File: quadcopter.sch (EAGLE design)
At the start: 69 parts, among them J4 AVR_SPI_PRG_6NS, M1 MOTOR_PADS, M2 MOTOR_PADS, M3 MOTOR_PADS, M4 MOTOR_PADS, U1 ATMEGA128RFA1

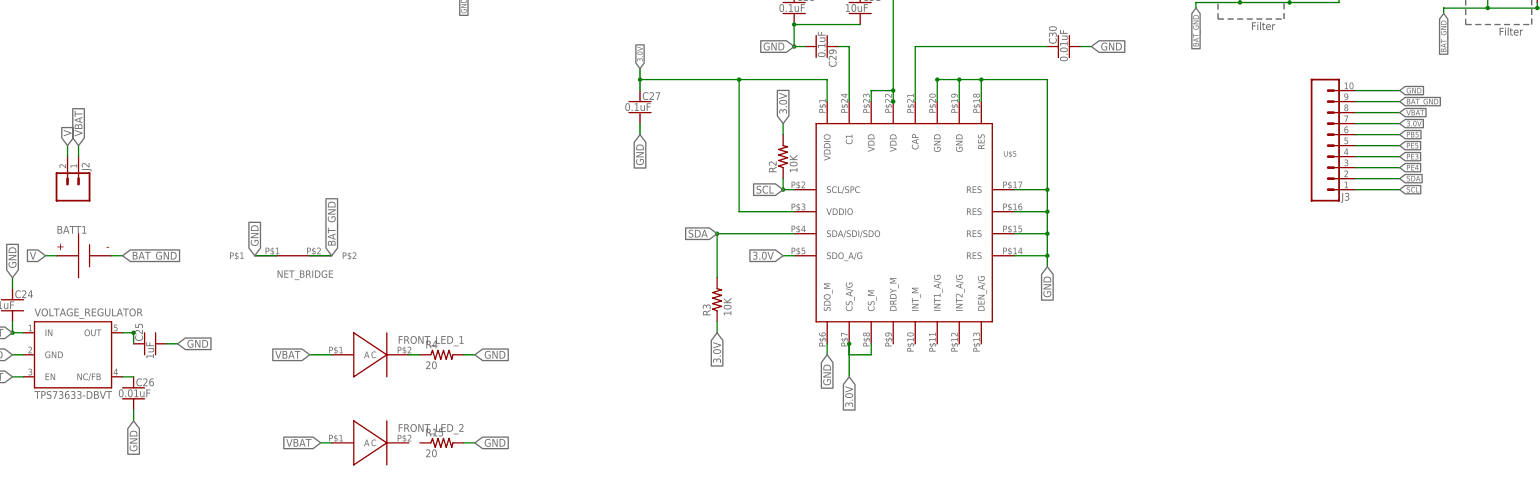
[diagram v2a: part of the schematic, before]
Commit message: Added all parts to board but have yet to run autorouter/set up the traces
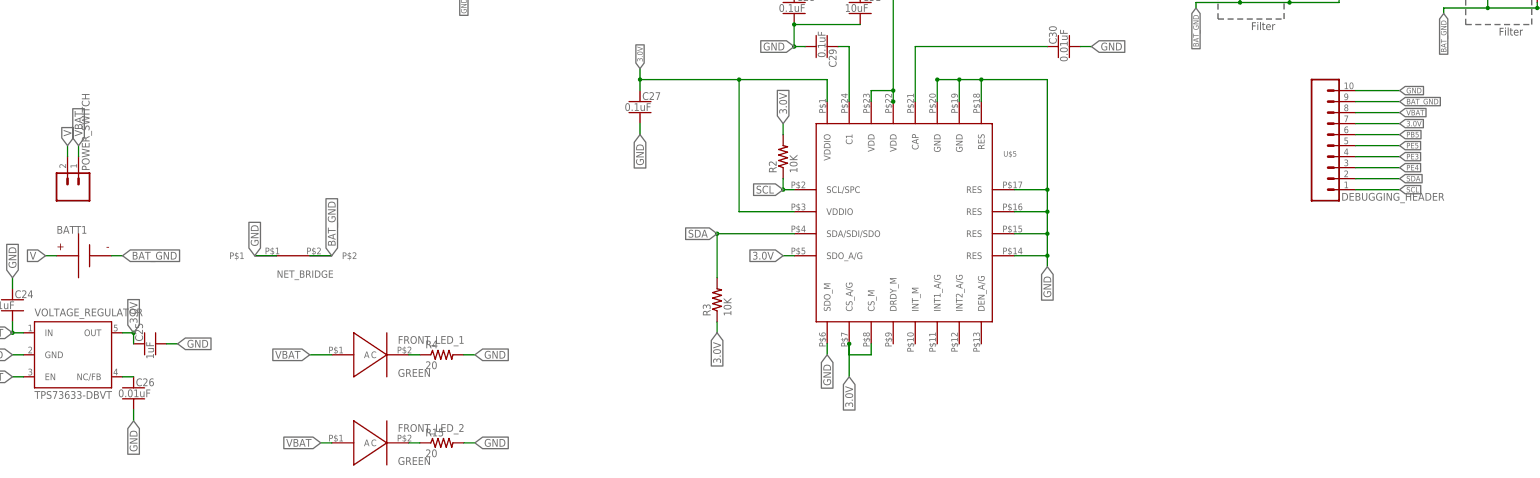
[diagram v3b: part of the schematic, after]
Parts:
- FRONT_LED_1, FRONT_LED_2: value (none) -> GREEN
- renumbered J2 to POWER_SWITCH, J3 to DEBUGGING_HEADER
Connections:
- new net N$5: FRONT_LED_2.C, R15.1
- net DTR: now also JP2.1
- net GND: now also JP2.6, JP3.6
- net RX0: now also JP2.3
- net RX1: now also JP3.2
- net TX0: now also JP2.2
- net TX1: now also JP3.3
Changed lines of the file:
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@@
 <setting verticaltext="up"/>
 </settings>
-<grid distance="0.05" unitdist="inch" unit="inch" style="lines" multiple="1" display="no" altdistance="0.01" altunitdist="inch" altunit="inch"/>
+<grid distance="0.1" unitdist="inch" unit="inch" style="lines" multiple="1" display="no" altdistance="0.01" altunitdist="inch" altunit="inch"/>
 <layers>
 <layer number="1" name="Top" color="4" fill="1" visible="no" active="no"/>
@@
 <part name="U$5" library="quadparts_jay" deviceset="IMU_497-14946-1-ND" device=""/>
 <part name="BATT1" library="quadparts_prebuilt" deviceset="BATTERY" device="-HUBSAN-W/HOLDER"/>
-<part name="J2" library="quadparts_jay" deviceset="MALE_HEADER_2POS" device="-2X1-0.1IN"/>
+<part name="POWER_SWITCH" library="quadparts_jay" deviceset="MALE_HEADER_2POS" device="-2X1-0.1IN"/>
 <part name="VOLTAGE_REGULATOR" library="quadparts_prebuilt" deviceset="TPS73633-DBVT" device=""/>
 <part name="NET_BRIDGE" library="quadparts_jay" deviceset="NET_BRIDGE" device=""/>
@@
 <part name="C6" library="quadparts_prebuilt" deviceset="CAPACITOR-NP_" device="SMD-2012-0805_CERAMIC-22PF" value="22pF"/>
 <part name="B2" library="quadparts_prebuilt" deviceset="BALUN" device="0805"/>
-<part name="J3" library="quadparts_prebuilt" deviceset="SIP-10_" device="TH-254X10-1"/>
-<part name="FRONT_LED_1" library="LEDs" deviceset="LED" device="-0805-GREEN"/>
-<part name="FRONT_LED_2" library="LEDs" deviceset="LED" device="-0805-GREEN"/>
+<part name="DEBUGGING_HEADER" library="quadparts_prebuilt" deviceset="SIP-10_" device="TH-254X10-1"/>
+<part name="FRONT_LED_1" library="LEDs" deviceset="LED" device="-0805-GREEN" value="GREEN"/>
+<part name="FRONT_LED_2" library="LEDs" deviceset="LED" device="-0805-GREEN" value="GREEN"/>
 <part name="R2" library="quadparts_prebuilt" deviceset="RESISTOR_" device="SMD-2012-0805-10K" value="10K"/>
 <part name="R3" library="quadparts_prebuilt" deviceset="RESISTOR_" device="SMD-2012-0805-10K" value="10K"/>
@@
 <instance part="U$5" gate="G$1" x="193.04" y="-45.72"/>
 <instance part="BATT1" gate="G$1" x="5.08" y="-53.34"/>
-<instance part="J2" gate="G$1" x="5.08" y="-40.64" rot="R90"/>
+<instance part="POWER_SWITCH" gate="G$1" x="5.08" y="-40.64" rot="R90"/>
 <instance part="VOLTAGE_REGULATOR" gate="G$1" x="-7.62" y="-83.82"/>
 <instance part="NET_BRIDGE" gate="G$1" x="53.34" y="-53.34"/>
@@
 <instance part="C6" gate="G$1" x="129.54" y="83.82" rot="R90"/>
 <instance part="B2" gate="G$1" x="142.24" y="81.28" rot="R180"/>
-<instance part="J3" gate="G$1" x="287.02" y="-40.64"/>
+<instance part="DEBUGGING_HEADER" gate="G$1" x="287.02" y="-40.64"/>
 <instance part="FRONT_LED_1" gate="G$1" x="71.12" y="-76.2"/>
 <instance part="FRONT_LED_2" gate="G$1" x="71.12" y="-96.52"/>
@@
 <wire x1="185.42" y1="158.75" x2="187.96" y2="158.75" width="0.1524" layer="91"/>
 <label x="187.96" y="158.75" size="1.27" layer="95" xref="yes"/>
+<pinref part="JP3" gate="G$1" pin="6"/>
 </segment>
 <segment>
@@
 </segment>
 <segment>
-<pinref part="J3" gate="G$1" pin="10"/>
+<pinref part="DEBUGGING_HEADER" gate="G$1" pin="10"/>
 <wire x1="297.18" y1="-15.24" x2="307.34" y2="-15.24" width="0.1524" layer="91"/>
 <label x="307.34" y="-15.24" size="1.27" layer="95" xref="yes"/>
@@
 <wire x1="123.19" y1="152.4" x2="125.73" y2="152.4" width="0.1524" layer="91"/>
 <label x="125.73" y="152.4" size="1.27" layer="95" xref="yes"/>
+<pinref part="JP2" gate="G$1" pin="6"/>
 </segment>
 <segment>
@@
 </segment>
 <segment>
-<pinref part="J3" gate="G$1" pin="5"/>
+<pinref part="DEBUGGING_HEADER" gate="G$1" pin="5"/>
 <wire x1="297.18" y1="-27.94" x2="307.34" y2="-27.94" width="0.1524" layer="91"/>
 <label x="307.34" y="-27.94" size="1.27" layer="95" xref="yes"/>
@@
 </segment>
 <segment>
-<pinref part="J3" gate="G$1" pin="3"/>
+<pinref part="DEBUGGING_HEADER" gate="G$1" pin="3"/>
 <wire x1="297.18" y1="-33.02" x2="307.34" y2="-33.02" width="0.1524" layer="91"/>
 <label x="307.34" y="-33.02" size="1.27" layer="95" xref="yes"/>
@@
 </segment>
 <segment>
-<pinref part="J3" gate="G$1" pin="4"/>
+<pinref part="DEBUGGING_HEADER" gate="G$1" pin="4"/>
 <wire x1="297.18" y1="-30.48" x2="307.34" y2="-30.48" width="0.1524" layer="91"/>
 <label x="307.34" y="-30.48" size="1.27" layer="95" xref="yes"/>
@@
 <wire x1="123.19" y1="142.24" x2="142.24" y2="142.24" width="0.1524" layer="91"/>
 <label x="142.24" y="142.24" size="1.27" layer="95" xref="yes"/>
+<pinref part="JP2" gate="G$1" pin="2"/>
 </segment>
 </net>
@@
 <wire x1="123.19" y1="144.78" x2="142.24" y2="144.78" width="0.1524" layer="91"/>
 <label x="142.24" y="144.78" size="1.27" layer="95" xref="yes"/>
+<pinref part="JP2" gate="G$1" pin="3"/>
 </segment>
 </net>
@@
 <wire x1="185.42" y1="151.13" x2="187.96" y2="151.13" width="0.1524" layer="91"/>
 <label x="187.96" y="151.13" size="1.27" layer="95" xref="yes"/>
+<pinref part="JP3" gate="G$1" pin="3"/>
 </segment>
 </net>
@@
 <wire x1="185.42" y1="148.59" x2="187.96" y2="148.59" width="0.1524" layer="91"/>
 <label x="187.96" y="148.59" size="1.27" layer="95" xref="yes"/>
+<pinref part="JP3" gate="G$1" pin="2"/>
 </segment>
 </net>
@@
 </segment>
 <segment>
-<pinref part="J3" gate="G$1" pin="2"/>
+<pinref part="DEBUGGING_HEADER" gate="G$1" pin="2"/>
 <wire x1="297.18" y1="-35.56" x2="307.34" y2="-35.56" width="0.1524" layer="91"/>
 <label x="307.34" y="-35.56" size="1.27" layer="95" xref="yes"/>
@@
 </segment>
 <segment>
-<pinref part="J3" gate="G$1" pin="1"/>
+<pinref part="DEBUGGING_HEADER" gate="G$1" pin="1"/>
 <wire x1="297.18" y1="-38.1" x2="307.34" y2="-38.1" width="0.1524" layer="91"/>
 <label x="307.34" y="-38.1" size="1.27" layer="95" xref="yes"/>
@@
 </segment>
 <segment>
-<pinref part="J3" gate="G$1" pin="6"/>
+<pinref part="DEBUGGING_HEADER" gate="G$1" pin="6"/>
 <wire x1="297.18" y1="-25.4" x2="307.34" y2="-25.4" width="0.1524" layer="91"/>
 <label x="307.34" y="-25.4" size="1.27" layer="95" xref="yes"/>
@@
 <pinref part="C15" gate="G$1" pin="1"/>
 <wire x1="130.81" y1="139.7" x2="123.19" y2="139.7" width="0.1524" layer="91"/>
+<pinref part="JP2" gate="G$1" pin="1"/>
 </segment>
 </net>
@@
 </segment>
 <segment>
-<pinref part="J2" gate="G$1" pin="1"/>
+<pinref part="POWER_SWITCH" gate="G$1" pin="1"/>
 <wire x1="2.54" y1="-30.48" x2="2.54" y2="-27.94" width="0.1524" layer="91"/>
 <label x="2.54" y="-27.94" size="1.778" layer="95" rot="R90" xref="yes"/>
 </segment>
 <segment>
-<pinref part="J3" gate="G$1" pin="8"/>
+<pinref part="DEBUGGING_HEADER" gate="G$1" pin="8"/>
 <wire x1="297.18" y1="-20.32" x2="307.34" y2="-20.32" width="0.1524" layer="91"/>
 <label x="307.34" y="-20.32" size="1.27" layer="95" xref="yes"/>
@@
 <wire x1="15.24" y1="-71.12" x2="15.24" y2="-73.66" width="0.1524" layer="91"/>
 <pinref part="C25" gate="G$1" pin="1"/>
+<label x="15.24" y="-71.12" size="1.778" layer="95" rot="R90" xref="yes"/>
 </segment>
 <segment>
@@
 </segment>
 <segment>
-<pinref part="J3" gate="G$1" pin="7"/>
+<pinref part="DEBUGGING_HEADER" gate="G$1" pin="7"/>
 <wire x1="297.18" y1="-22.86" x2="307.34" y2="-22.86" width="0.1524" layer="91"/>
 <label x="307.34" y="-22.86" size="1.27" layer="95" xref="yes"/>
@@
 </segment>
 <segment>
-<pinref part="J3" gate="G$1" pin="9"/>
+<pinref part="DEBUGGING_HEADER" gate="G$1" pin="9"/>
 <wire x1="297.18" y1="-17.78" x2="307.34" y2="-17.78" width="0.1524" layer="91"/>
 <label x="307.34" y="-17.78" size="1.27" layer="95" xref="yes"/>
@@
 </segment>
 <segment>
-<pinref part="J2" gate="G$1" pin="2"/>
+<pinref part="POWER_SWITCH" gate="G$1" pin="2"/>
 <wire x1="0" y1="-30.48" x2="0" y2="-27.94" width="0.1524" layer="91"/>
 <label x="0" y="-27.94" size="1.778" layer="95" rot="R90" xref="yes"/>
@@
 </segment>
 </net>
+<net name="N$5" class="0">
+<segment>
+<pinref part="FRONT_LED_2" gate="G$1" pin="C"/>
+<pinref part="R15" gate="G$1" pin="1"/>
+<wire x1="78.74" y1="-96.52" x2="81.28" y2="-96.52" width="0.1524" layer="91"/>
+</segment>
+</net>
 </nets>
 </sheet>
 </sheets>
+<errors>
+</errors>
 </schematic>
 </drawing>

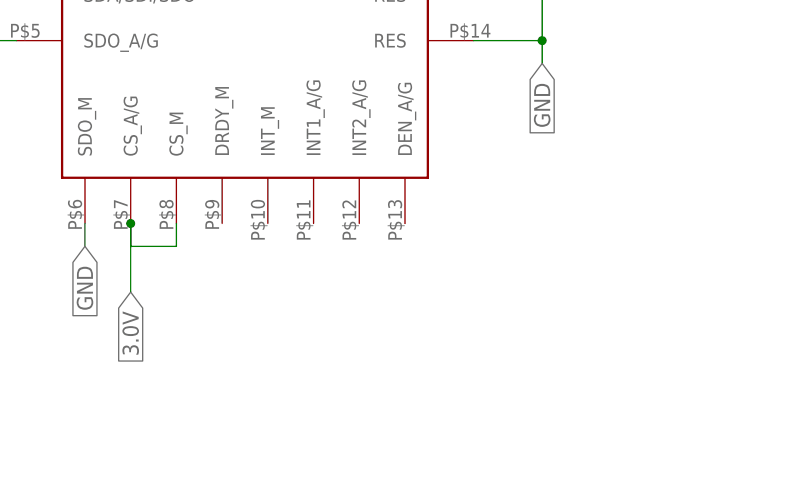
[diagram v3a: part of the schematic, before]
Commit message: Fixed some schematic things, still need to fix swanson notes and the motor drivers
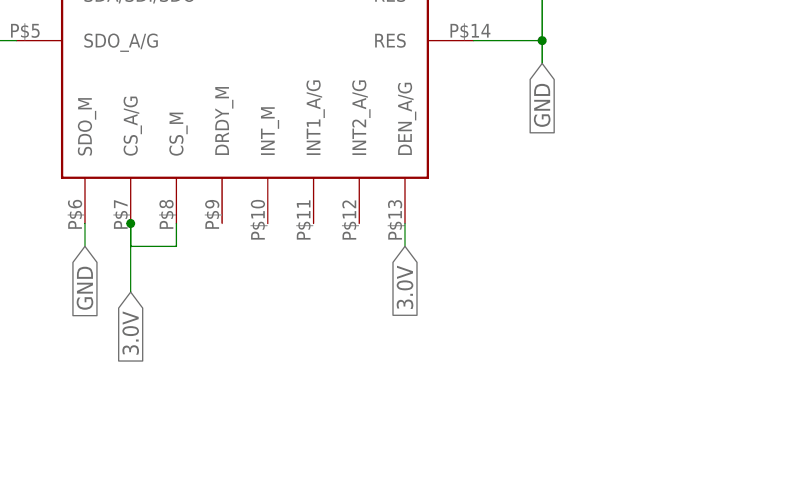
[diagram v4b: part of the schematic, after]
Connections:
- net 3.0V: now also U$5.DEN_A/G
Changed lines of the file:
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@@
 <label x="165.1" y="-22.86" size="1.778" layer="95" rot="R90" xref="yes"/>
+</segment>
+<segment>
+<pinref part="U$5" gate="G$1" pin="DEN_A/G"/>
+<wire x1="210.82" y1="-73.66" x2="210.82" y2="-76.2" width="0.1524" layer="91"/>
+<label x="210.82" y="-76.2" size="1.778" layer="95" rot="R270" xref="yes"/>
 </segment>
 </net>

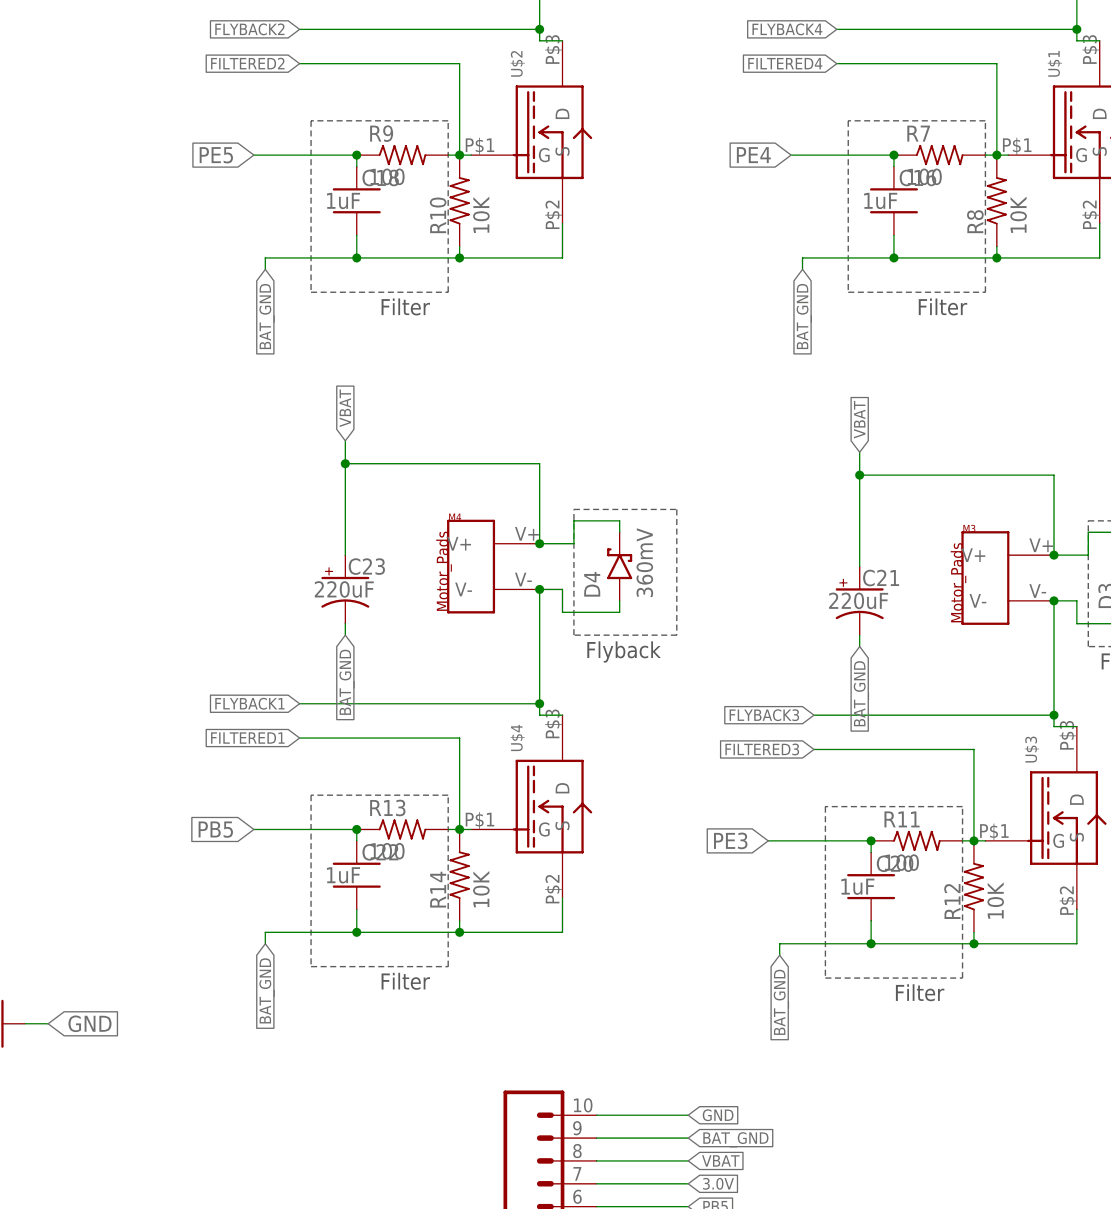
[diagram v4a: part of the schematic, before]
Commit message: Modify Motor Driver and check off components on swanson_design_review
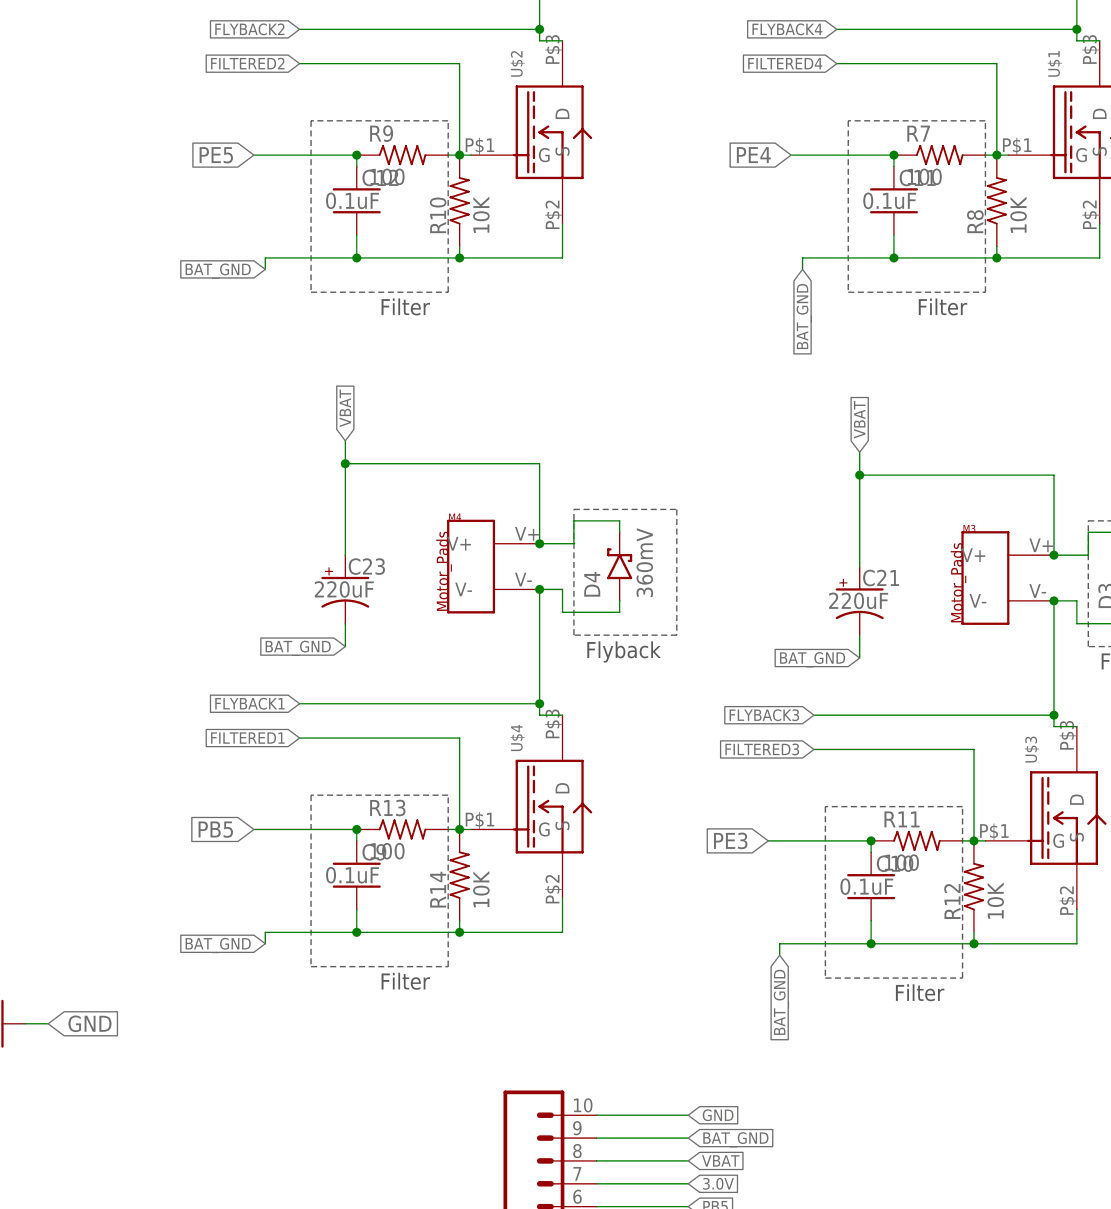
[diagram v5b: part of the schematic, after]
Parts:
- removed C16, C18, C20, C22: 1uF, quadparts_prebuilt:CAPACITOR-NP_SMD-2012-0805_CERAMIC-1UF
- added C10, C11, C12, C9: 0.1uF, quadparts_prebuilt:CAPACITOR-NP_SMD-2012-0805_CERAMIC-0.1UF
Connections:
- net BAT_GND: now also C10.2, C11.2, C12.2, C9.2; no longer C16.2, C18.2, C20.2, C22.2
- net PB5: now also C9.1; no longer C22.1
- net PE3: now also C10.1; no longer C20.1
- net PE4: now also C11.1; no longer C16.1
- net PE5: now also C12.1; no longer C18.1
